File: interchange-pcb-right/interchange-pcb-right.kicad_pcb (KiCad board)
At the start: 2 copper layers, 175.6 x 104 mm, 165 parts, among them J1 Conn_01x04, J2 Conn_01x04, J3 TRRS_L, J4 TRRS_R, J5 SSD1306, SW1 RotaryEncoder, U1 Seeeduino Xiao rp2040, U2 PCA9555PW, U3 PCA9555PW, U4 ADS1110, U5 SN74AHCT125PWR, U6 TCA4307DGKR

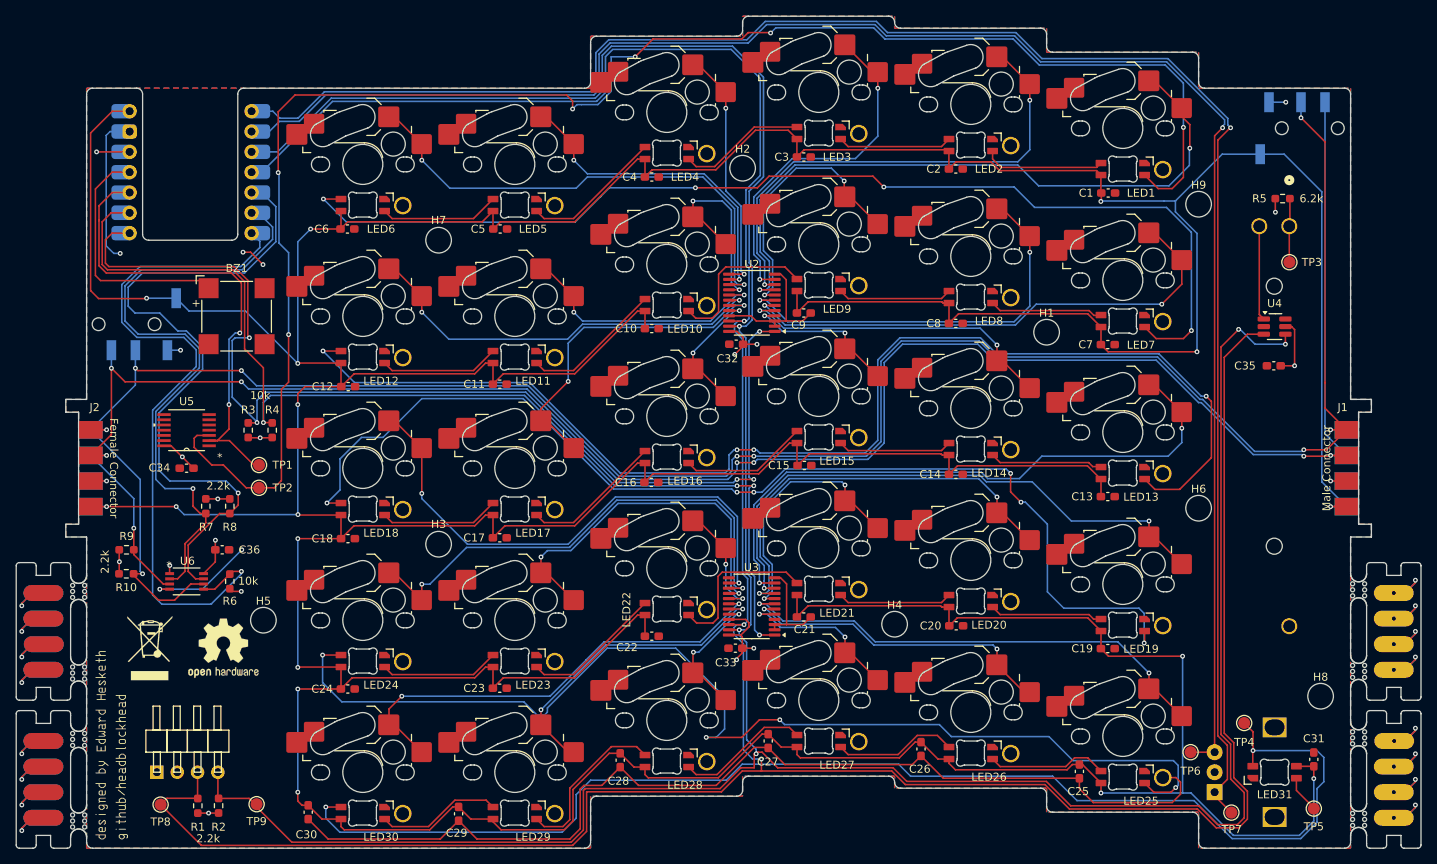
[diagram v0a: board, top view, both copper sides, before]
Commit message: feat: create schematic for interchange-pcb-hackpad
and fix minor spacing issues with capaicitors in interchange-pcb-right
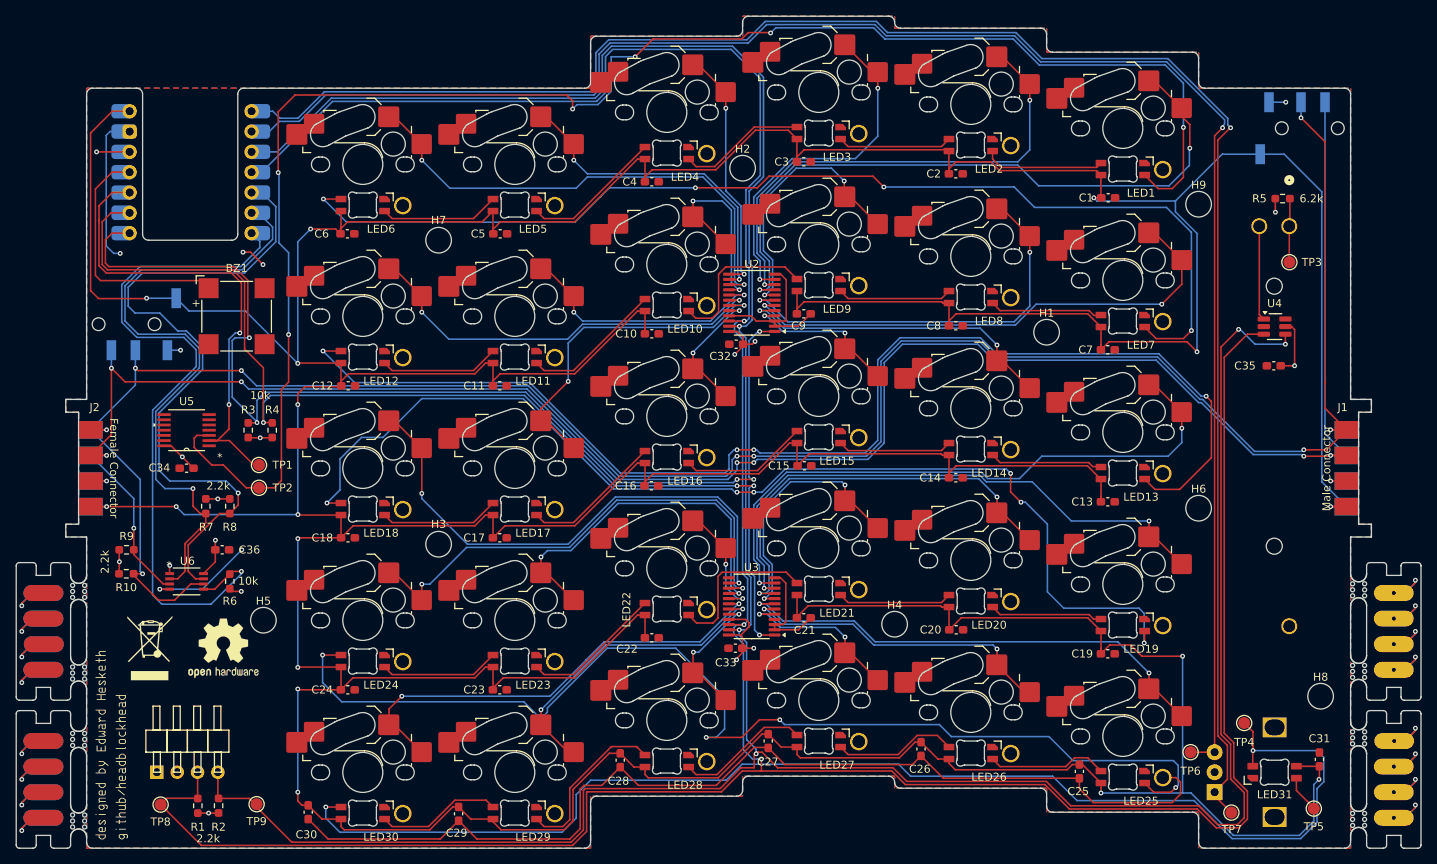
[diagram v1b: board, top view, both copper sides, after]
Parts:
- moved C31 0.70 mm to (224.1, 138.9)
- moved C10 0.65 mm to (140.7, 85.7)
- moved C13 0.65 mm to (197.7, 106.7)
- moved C19 0.65 mm to (197.7, 125.7)
- moved C7 0.65 mm to (197.7, 87.7)
- moved C1 0.60 mm to (197.7, 68.7)
- moved C2 0.60 mm to (178.7, 65.7)
- moved C4 0.60 mm to (140.7, 66.7)
- moved C5 0.60 mm to (121.7, 73.2)
- moved C6 0.60 mm to (102.6, 73.2)
- moved C3 0.60 mm to (159.7, 64.2)
- moved C20 0.50 mm to (178.7, 122.7)
- moved C14 0.43 mm to (178.7, 103.7)
- moved C16 0.43 mm to (140.6, 104.7)
- moved C8 0.30 mm to (178.7, 84.7)
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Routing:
- net VBUS: track 914.9 -> 928.1 mm
- net GND: track 206.5 -> 209.6 mm

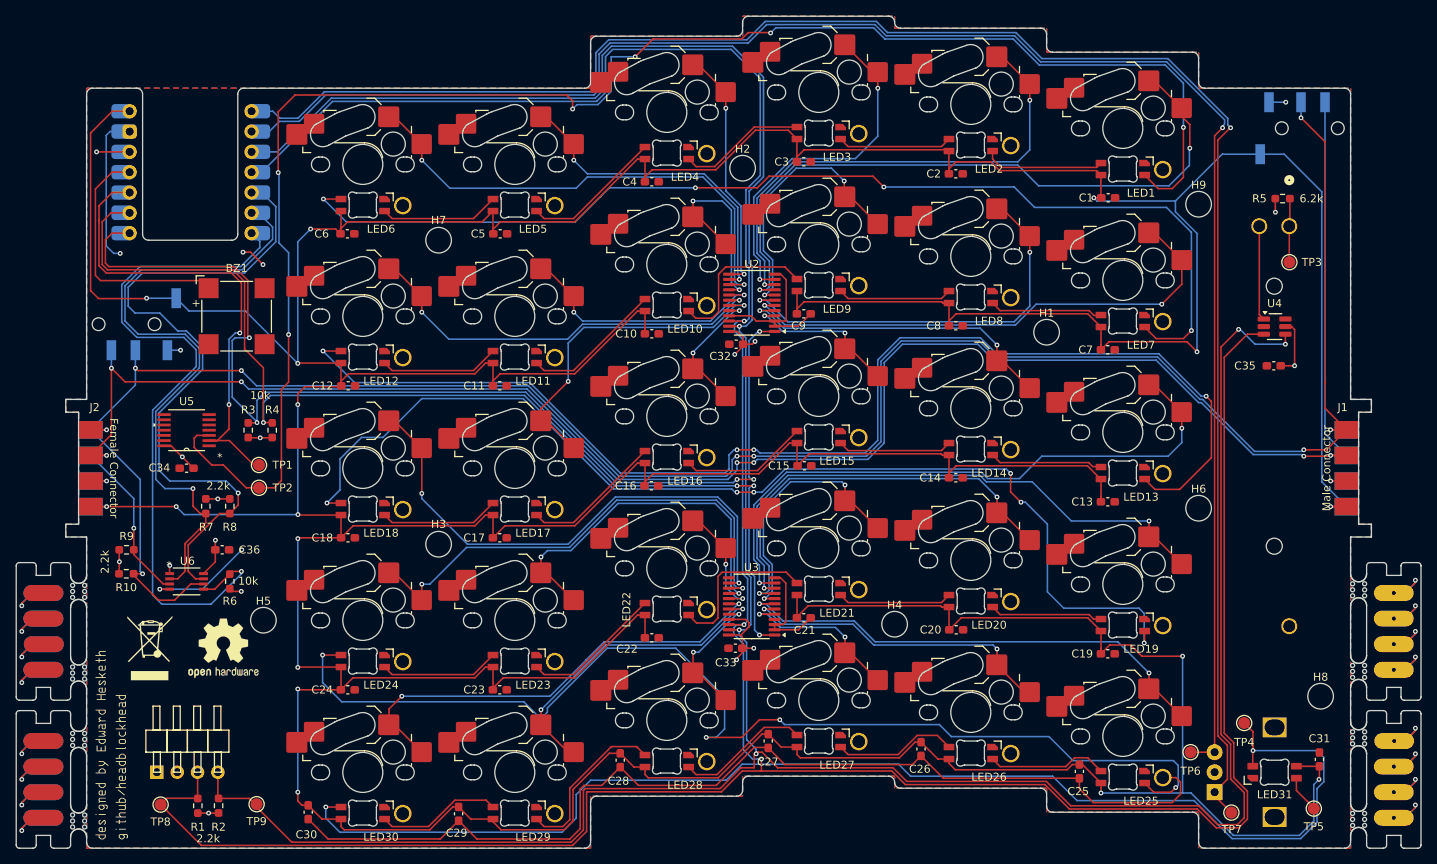
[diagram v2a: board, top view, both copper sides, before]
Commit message: wip: add reverse polarity protection and fix buzzer
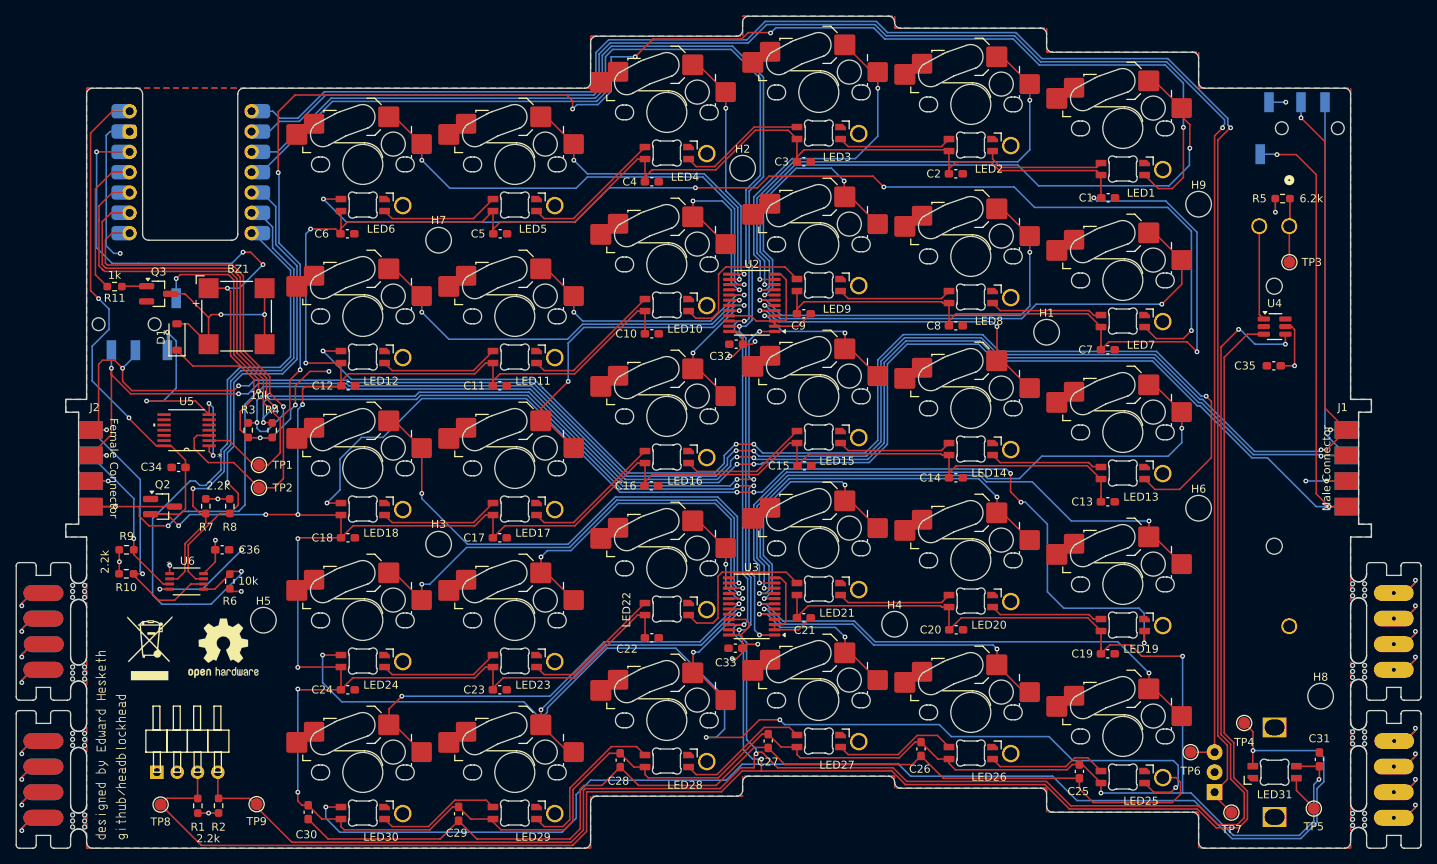
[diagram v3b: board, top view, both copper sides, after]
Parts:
- added D1: 1N4448W, Diode_SMD:D_SOD-123, F.Cu at (81.3, 86.1)
- added Q2: Q_PMOS_GSD, Package_TO_SOT_SMD:SOT-23_Handsoldering, F.Cu at (79.5, 107.3)
- added Q3: Q_NPN_BEC, Package_TO_SOT_SMD:SOT-23_Handsoldering, F.Cu at (79.0, 80.7)
- added R11: 1k, Resistor_SMD:R_0603_1608Metric_Pad0.98x0.95mm_HandSolder, F.Cu at (73.5, 79.8)
- moved C34 1.00 mm to (81.5, 102.4)
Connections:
- BZ1 pad 1: /BUZZER -> +3V3
- BZ1 pad 2: GND -> Net-(BZ1--)
- C1 pad 2: VBUS -> +5V
- C10 pad 2: VBUS -> +5V
- C11 pad 2: VBUS -> +5V
- C12 pad 2: VBUS -> +5V
- C13 pad 2: VBUS -> +5V
- C14 pad 2: VBUS -> +5V
- C15 pad 2: VBUS -> +5V
- C16 pad 2: VBUS -> +5V
- C17 pad 2: VBUS -> +5V
- C18 pad 2: VBUS -> +5V
- C19 pad 2: VBUS -> +5V
- C2 pad 2: VBUS -> +5V
- C20 pad 2: VBUS -> +5V
- C21 pad 2: VBUS -> +5V
- C22 pad 2: VBUS -> +5V
- C23 pad 2: VBUS -> +5V
- C24 pad 2: VBUS -> +5V
- C25 pad 2: VBUS -> +5V
- C26 pad 2: VBUS -> +5V
- C27 pad 2: VBUS -> +5V
- C28 pad 2: VBUS -> +5V
- C29 pad 2: VBUS -> +5V
- C3 pad 2: VBUS -> +5V
- C30 pad 2: VBUS -> +5V
- C31 pad 2: VBUS -> +5V
- C34 pad 2: +3V3 -> +5V
- C4 pad 2: VBUS -> +5V
- C5 pad 2: VBUS -> +5V
- C6 pad 2: VBUS -> +5V
- C7 pad 2: VBUS -> +5V
- C8 pad 2: VBUS -> +5V
- C9 pad 2: VBUS -> +5V
- LED1 pad 1: VBUS -> +5V
- LED10 pad 1: VBUS -> +5V
- LED11 pad 1: VBUS -> +5V
- LED12 pad 1: VBUS -> +5V
- LED13 pad 1: VBUS -> +5V
- LED14 pad 1: VBUS -> +5V
- LED15 pad 1: VBUS -> +5V
- LED16 pad 1: VBUS -> +5V
- LED17 pad 1: VBUS -> +5V
- LED18 pad 1: VBUS -> +5V
- LED19 pad 1: VBUS -> +5V
- LED2 pad 1: VBUS -> +5V
- LED20 pad 1: VBUS -> +5V
- LED21 pad 1: VBUS -> +5V
- LED22 pad 1: VBUS -> +5V
- LED23 pad 1: VBUS -> +5V
- LED24 pad 1: VBUS -> +5V
- LED25 pad 1: VBUS -> +5V
- LED26 pad 1: VBUS -> +5V
- LED27 pad 1: VBUS -> +5V
- LED28 pad 1: VBUS -> +5V
- LED29 pad 1: VBUS -> +5V
- LED3 pad 1: VBUS -> +5V
- LED30 pad 1: VBUS -> +5V
- LED31 pad 1: VBUS -> +5V
- LED4 pad 1: VBUS -> +5V
- LED5 pad 1: VBUS -> +5V
- LED6 pad 1: VBUS -> +5V
- LED7 pad 1: VBUS -> +5V
- LED8 pad 1: VBUS -> +5V
- LED9 pad 1: VBUS -> +5V
- U1 pad 8: VBUS -> +5V
- U5 pad 14: +3V3 -> +5V
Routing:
- net +5V: track 0.00 -> 859.8 mm, vias 0 -> 17
- net VBUS: track 928.1 -> 284.6 mm, vias 17 -> 8
- net +3V3: track 57.8 -> 138.5 mm, vias 17 -> 19
- net GND: track 209.6 -> 244.1 mm, vias 7 -> 11
- net Net-(BZ1--): track 0.00 -> 29.2 mm, vias 0 -> 2
- net /I2C1_SDA: track 86.9 -> 63.2 mm
- net /I2C1_SCL: track 79.4 -> 61.1 mm
- net /BUZZER: track 30.8 -> 18.0 mm
- net /I2C1_RDY: track 88.9 -> 78.0 mm
- net /I2C_BUS_SDA: track 273.9 -> 281.1 mm
- net /SHIFTER_INPUT: track 60.7 -> 64.9 mm, vias 2 -> 0
- net /I2C_BUS_SCL: track 265.6 -> 268.8 mm, vias 8 -> 7
- net Net-(Q3-B): track 0.00 -> 3.11 mm
- net /EXPANDER1_INT: track 138.8 -> 141.7 mm
- net /EXPANDER2_INT: track 138.0 -> 139.5 mm, vias 4 -> 5
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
